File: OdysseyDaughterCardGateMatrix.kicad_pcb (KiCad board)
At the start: 2 copper layers, 47.8 x 46.6 mm, 17 parts, among them X1 OdysseyDaughterCard

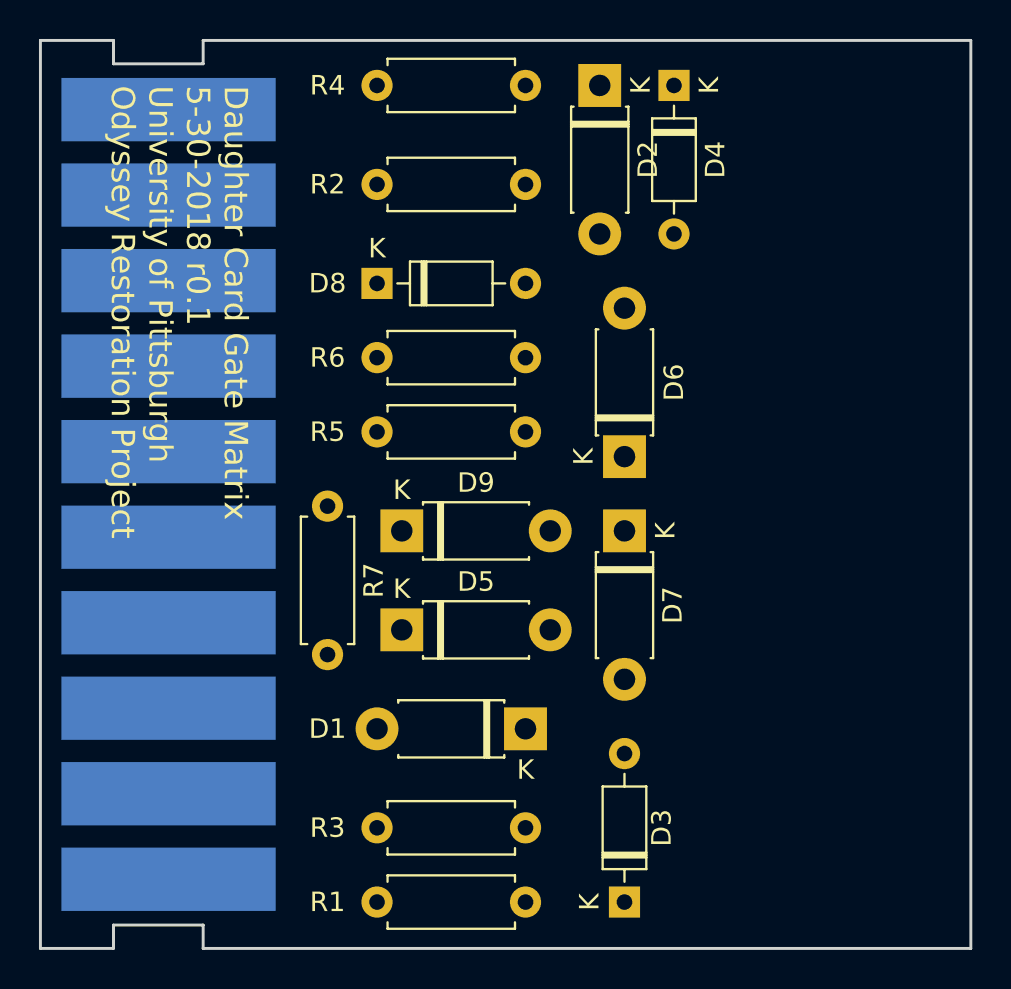
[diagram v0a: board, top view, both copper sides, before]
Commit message: Routed gate matrix
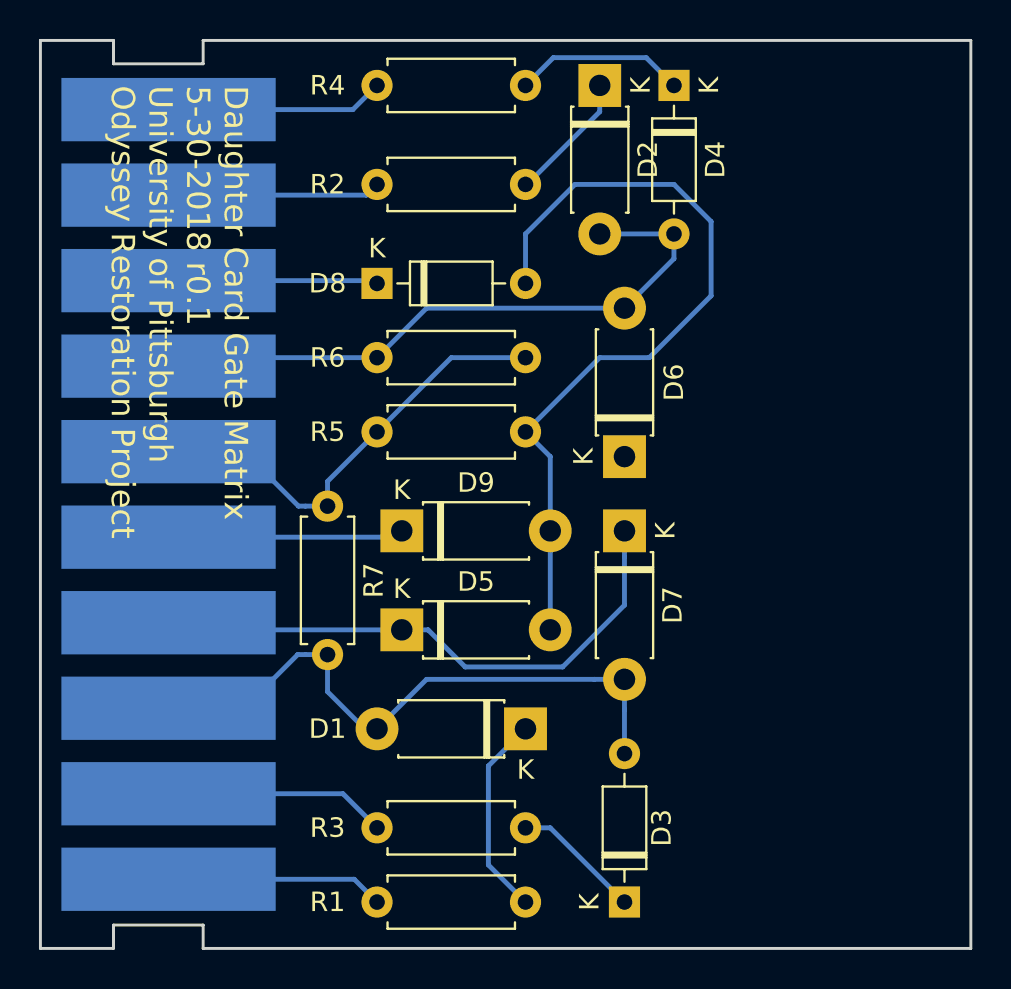
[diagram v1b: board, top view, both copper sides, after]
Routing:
- net Net-(D5-Pad2): track 0.00 -> 40.8 mm
- net /Card7: track 0.00 -> 33.3 mm
- net /Card3: track 0.00 -> 32.1 mm
- net /Card4: track 0.00 -> 29.5 mm
- net /Card6: track 0.00 -> 23.4 mm
- net /Card5: track 0.00 -> 12.1 mm
- net /Card2: track 0.00 -> 11.4 mm
- net /Card10: track 0.00 -> 11.2 mm
- net /Card1: track 0.00 -> 11.2 mm
- net /Card9: track 0.00 -> 10.9 mm
- net /Card8: track 0.00 -> 10.8 mm
- net Net-(D1-Pad1): track 0.00 -> 10.5 mm
- net Net-(D4-Pad1): track 0.00 -> 8.80 mm
- net Net-(D2-Pad1): track 0.00 -> 6.71 mm
- net Net-(D3-Pad1): track 0.00 -> 6.66 mm
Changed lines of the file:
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@@
     (thickness 1.6)
     (drawings 13)
-    (tracks 0)
+    (tracks 69)
     (zones 0)
     (modules 17)
@@
   )
   (gr_line (start 122.425 124.3) (end 122.425 77.7) (layer Edge.Cuts) (width 0.15))
+  (segment (start 145.415 120.015) (end 145.415 114.935) (width 0.25) (layer B.Cu) (net 1))
+  (segment (start 147.32 121.92) (end 145.415 120.015) (width 0.25) (layer B.Cu) (net 1))
+  (segment (start 145.415 114.935) (end 147.32 113.03) (width 0.25) (layer B.Cu) (net 1))
+  (segment (start 152.4 110.49) (end 152.4 112.045634) (width 0.25) (layer B.Cu) (net 2))
+  (segment (start 152.4 112.045634) (end 152.4 114.3) (width 0.25) (layer B.Cu) (net 2))
+  (segment (start 137.16 111.125) (end 139.065 113.03) (width 0.25) (layer B.Cu) (net 2))
+  (segment (start 137.16 109.22) (end 137.16 111.125) (width 0.25) (layer B.Cu) (net 2))
+  (segment (start 139.065 113.03) (end 139.7 113.03) (width 0.25) (layer B.Cu) (net 2))
+  (segment (start 142.24 110.49) (end 150.844366 110.49) (width 0.25) (layer B.Cu) (net 2))
+  (segment (start 139.7 113.03) (end 142.24 110.49) (width 0.25) (layer B.Cu) (net 2))
+  (segment (start 150.844366 110.49) (end 152.4 110.49) (width 0.25) (layer B.Cu) (net 2))
+  (segment (start 129 111.972216) (end 132.875 111.972216) (width 0.25) (layer B.Cu) (net 2))
+  (segment (start 132.875 111.972216) (end 135.627216 109.22) (width 0.25) (layer B.Cu) (net 2))
+  (segment (start 135.627216 109.22) (end 136.02863 109.22) (width 0.25) (layer B.Cu) (net 2))
+  (segment (start 136.02863 109.22) (end 137.16 109.22) (width 0.25) (layer B.Cu) (net 2))
+  (segment (start 139.7 93.98) (end 129.436664 93.98) (width 0.25) (layer B.Cu) (net 3))
+  (segment (start 129.436664 93.98) (end 129 94.416664) (width 0.25) (layer B.Cu) (net 3))
+  (segment (start 152.4 91.44) (end 142.24 91.44) (width 0.25) (layer B.Cu) (net 3))
+  (segment (start 142.24 91.44) (end 139.7 93.98) (width 0.25) (layer B.Cu) (net 3))
+  (segment (start 154.94 87.63) (end 154.94 88.9) (width 0.25) (layer B.Cu) (net 3))
+  (segment (start 154.94 88.9) (end 152.4 91.44) (width 0.25) (layer B.Cu) (net 3))
+  (segment (start 154.94 87.63) (end 151.13 87.63) (width 0.25) (layer B.Cu) (net 3))
+  (segment (start 151.13 80.01) (end 151.13 81.36) (width 0.25) (layer B.Cu) (net 4))
+  (segment (start 151.13 81.36) (end 147.4 85.09) (width 0.25) (layer B.Cu) (net 4))
+  (segment (start 147.4 85.09) (end 147.32 85.09) (width 0.25) (layer B.Cu) (net 4))
+  (segment (start 147.32 118.11) (end 148.59 118.11) (width 0.25) (layer B.Cu) (net 5))
+  (segment (start 148.59 118.11) (end 152.4 121.92) (width 0.25) (layer B.Cu) (net 5))
+  (segment (start 153.514999 78.584999) (end 154.94 80.01) (width 0.25) (layer B.Cu) (net 6))
+  (segment (start 147.32 80.01) (end 148.745001 78.584999) (width 0.25) (layer B.Cu) (net 6))
+  (segment (start 148.745001 78.584999) (end 153.514999 78.584999) (width 0.25) (layer B.Cu) (net 6))
+  (segment (start 142.32 107.95) (end 144.225 109.855) (width 0.25) (layer B.Cu) (net 7))
+  (segment (start 140.97 107.95) (end 142.32 107.95) (width 0.25) (layer B.Cu) (net 7))
+  (segment (start 144.225 109.855) (end 149.225 109.855) (width 0.25) (layer B.Cu) (net 7))
+  (segment (start 149.225 109.855) (end 152.4 106.68) (width 0.25) (layer B.Cu) (net 7))
+  (segment (start 152.4 106.68) (end 152.4 104.22) (width 0.25) (layer B.Cu) (net 7))
+  (segment (start 152.4 104.22) (end 152.4 102.87) (width 0.25) (layer B.Cu) (net 7))
+  (segment (start 140.97 107.95) (end 129.366672 107.95) (width 0.25) (layer B.Cu) (net 7))
+  (segment (start 129.366672 107.95) (end 129 107.583328) (width 0.25) (layer B.Cu) (net 7))
+  (segment (start 156.845 90.805) (end 153.67 93.98) (width 0.25) (layer B.Cu) (net 8))
+  (segment (start 156.845 86.995) (end 156.845 90.805) (width 0.25) (layer B.Cu) (net 8))
+  (segment (start 154.94 85.09) (end 156.845 86.995) (width 0.25) (layer B.Cu) (net 8))
+  (segment (start 149.86 85.09) (end 154.94 85.09) (width 0.25) (layer B.Cu) (net 8))
+  (segment (start 147.32 90.17) (end 147.32 87.63) (width 0.25) (layer B.Cu) (net 8))
+  (segment (start 147.32 87.63) (end 149.86 85.09) (width 0.25) (layer B.Cu) (net 8))
+  (segment (start 153.67 93.98) (end 151.13 93.98) (width 0.25) (layer B.Cu) (net 8))
+  (segment (start 151.13 93.98) (end 147.32 97.79) (width 0.25) (layer B.Cu) (net 8))
+  (segment (start 148.59 102.87) (end 148.59 107.95) (width 0.25) (layer B.Cu) (net 8))
+  (segment (start 147.32 97.79) (end 148.59 99.06) (width 0.25) (layer B.Cu) (net 8))
+  (segment (start 148.59 99.06) (end 148.59 102.87) (width 0.25) (layer B.Cu) (net 8))
+  (segment (start 129 90.027776) (end 139.557776 90.027776) (width 0.25) (layer B.Cu) (net 9))
+  (segment (start 139.557776 90.027776) (end 139.7 90.17) (width 0.25) (layer B.Cu) (net 9))
+  (segment (start 129 103.19444) (end 140.64556 103.19444) (width 0.25) (layer B.Cu) (net 10))
+  (segment (start 140.64556 103.19444) (end 140.97 102.87) (width 0.25) (layer B.Cu) (net 10))
+  (segment (start 129 120.749992) (end 138.529992 120.749992) (width 0.25) (layer B.Cu) (net 11))
+  (segment (start 138.529992 120.749992) (end 139.7 121.92) (width 0.25) (layer B.Cu) (net 11))
+  (segment (start 129 85.638888) (end 139.151112 85.638888) (width 0.25) (layer B.Cu) (net 12))
+  (segment (start 139.151112 85.638888) (end 139.7 85.09) (width 0.25) (layer B.Cu) (net 12))
+  (segment (start 129 116.361104) (end 137.951104 116.361104) (width 0.25) (layer B.Cu) (net 13))
+  (segment (start 137.951104 116.361104) (end 139.7 118.11) (width 0.25) (layer B.Cu) (net 13))
+  (segment (start 129 81.25) (end 138.46 81.25) (width 0.25) (layer B.Cu) (net 14))
+  (segment (start 138.46 81.25) (end 139.7 80.01) (width 0.25) (layer B.Cu) (net 14))
+  (segment (start 139.7 97.79) (end 143.51 93.98) (width 0.25) (layer B.Cu) (net 15))
+  (segment (start 143.51 93.98) (end 147.32 93.98) (width 0.25) (layer B.Cu) (net 15))
+  (segment (start 137.16 101.6) (end 137.16 100.33) (width 0.25) (layer B.Cu) (net 15))
+  (segment (start 137.16 100.33) (end 139.7 97.79) (width 0.25) (layer B.Cu) (net 15))
+  (segment (start 129 98.805552) (end 132.875 98.805552) (width 0.25) (layer B.Cu) (net 15))
+  (segment (start 132.875 98.805552) (end 135.669448 101.6) (width 0.25) (layer B.Cu) (net 15))
+  (segment (start 135.669448 101.6) (end 136.02863 101.6) (width 0.25) (layer B.Cu) (net 15))
+  (segment (start 136.02863 101.6) (end 137.16 101.6) (width 0.25) (layer B.Cu) (net 15))
 )

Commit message: Shrink PCB
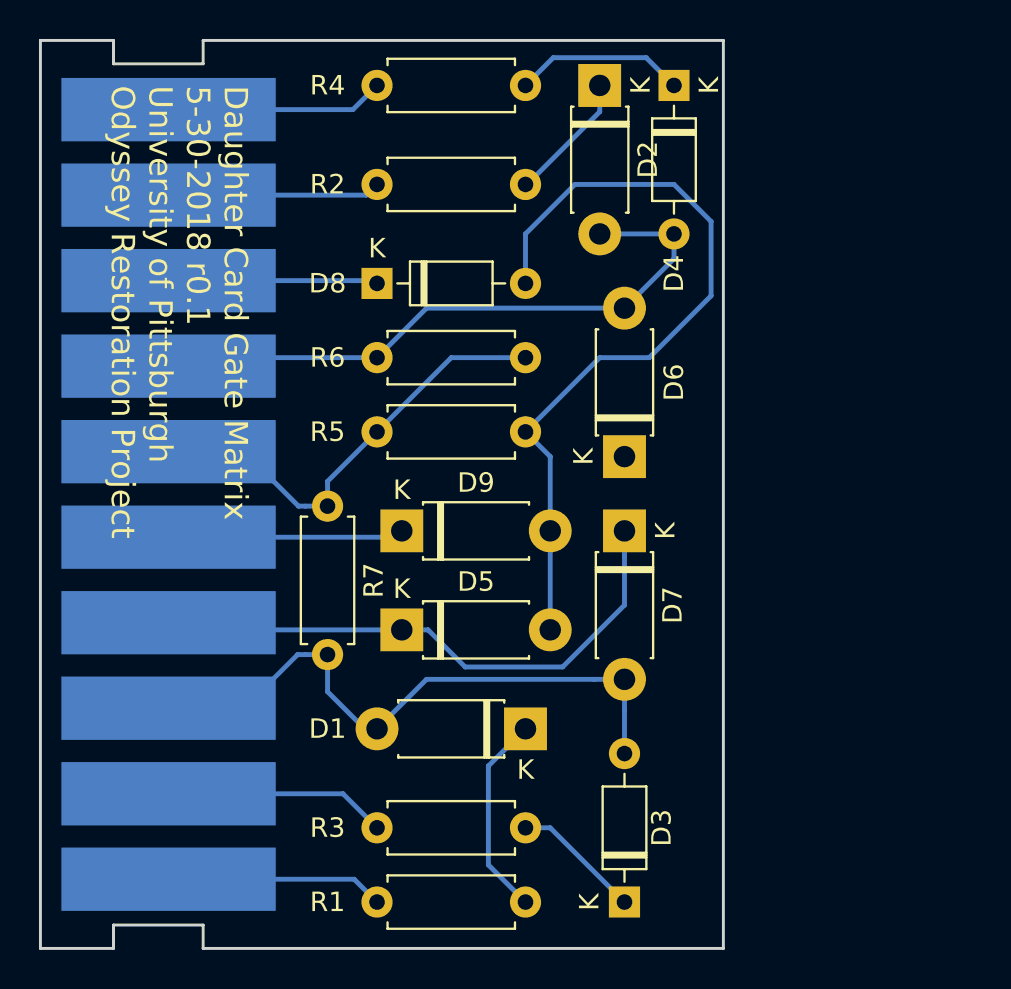
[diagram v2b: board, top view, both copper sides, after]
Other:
- board size 47.8 x 46.6 mm -> 35 x 46.6 mm
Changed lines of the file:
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@@
     (descr "D, DO-35_SOD27 series, Axial, Horizontal, pin pitch=7.62mm, , length*diameter=4*2mm^2, , http://www.diodes.com/_files/packages/DO-35.pdf")
     (tags "D DO-35_SOD27 series Axial Horizontal pin pitch 7.62mm  length 4mm diameter 2mm")
-    (fp_text reference D4 (at 3.81 -2.12 270) (layer F.SilkS)
+    (fp_text reference D4 (at 9.652 0 270) (layer F.SilkS)
       (effects (font (size 1 1) (thickness 0.15)))
     )
@@
     )
   )
-  (gr_line (start 170.175 77.7) (end 170.175 124.3) (layer Edge.Cuts) (width 0.15))
+  (gr_line (start 157.475 77.7) (end 157.475 124.3) (layer Edge.Cuts) (width 0.15))
   (gr_line (start 126.175 77.7) (end 122.425 77.7) (layer Edge.Cuts) (width 0.15))
   (gr_line (start 126.175 78.9) (end 126.175 77.7) (layer Edge.Cuts) (width 0.15))
   (gr_line (start 130.775 78.9) (end 126.175 78.9) (layer Edge.Cuts) (width 0.15))
   (gr_line (start 130.775 77.7) (end 130.775 78.9) (layer Edge.Cuts) (width 0.15))
-  (gr_line (start 170.175 77.7) (end 130.775 77.7) (layer Edge.Cuts) (width 0.15))
-  (gr_line (start 130.775 124.3) (end 170.175 124.3) (layer Edge.Cuts) (width 0.15))
+  (gr_line (start 157.475 77.7) (end 130.775 77.7) (layer Edge.Cuts) (width 0.15))
+  (gr_line (start 130.775 124.3) (end 157.475 124.3) (layer Edge.Cuts) (width 0.15))
   (gr_line (start 130.775 123.1) (end 130.775 124.3) (layer Edge.Cuts) (width 0.15))
   (gr_line (start 126.175 123.1) (end 130.775 123.1) (layer Edge.Cuts) (width 0.15))
